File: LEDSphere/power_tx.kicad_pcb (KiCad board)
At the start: 2 copper layers, 124 x 120 mm, 90 parts, among them J1 USB_C_Receptacle_USB2.0, M1 Motor_DC, Q1 BSS138, Q2 BSS138, Q3 BSS138, Q4 BSS138, Q5 BSS138, Q6 BSS138, Q7 Si2319CDS, Q8 Si2319CDS, U1 4017, U2 CH221K, U3 TPS54302, U4 SG3525, U8 UCC27714DR

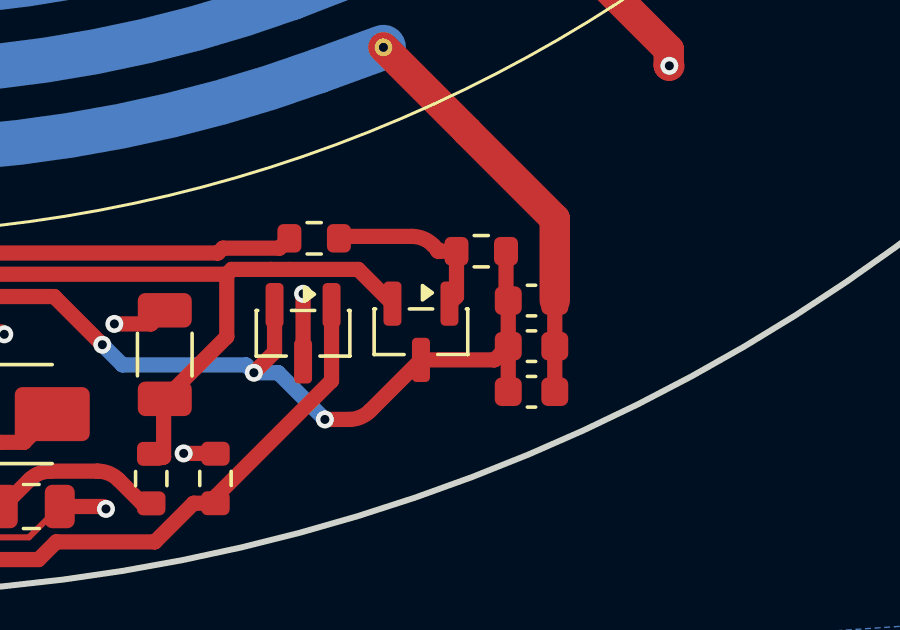
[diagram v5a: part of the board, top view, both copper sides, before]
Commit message: Updated Resonance FRQ + Test Points Added
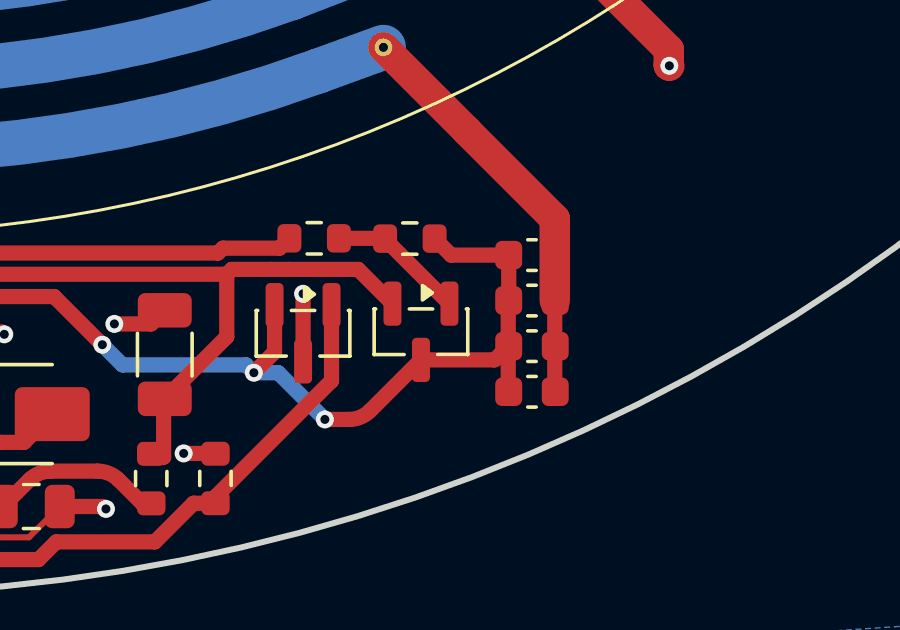
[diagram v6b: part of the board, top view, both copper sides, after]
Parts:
- added C29: 68nF, Capacitor_SMD:C_0603_1608Metric, F.Cu at (159.6, 144.8)
- L2: value 8.1 uH -> 5.8 uH
- moved R31 2.42 mm to (155.5, 144.3)
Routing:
- net /HS: track 47.7 -> 50.2 mm
- net /FET_HI: track 6.00 -> 4.60 mm

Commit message: Most Recent TX Board Changes
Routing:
- net +12V: track 184.6 -> 158.8 mm
- net Net-(U8-LI): track 1.88 -> 7.59 mm

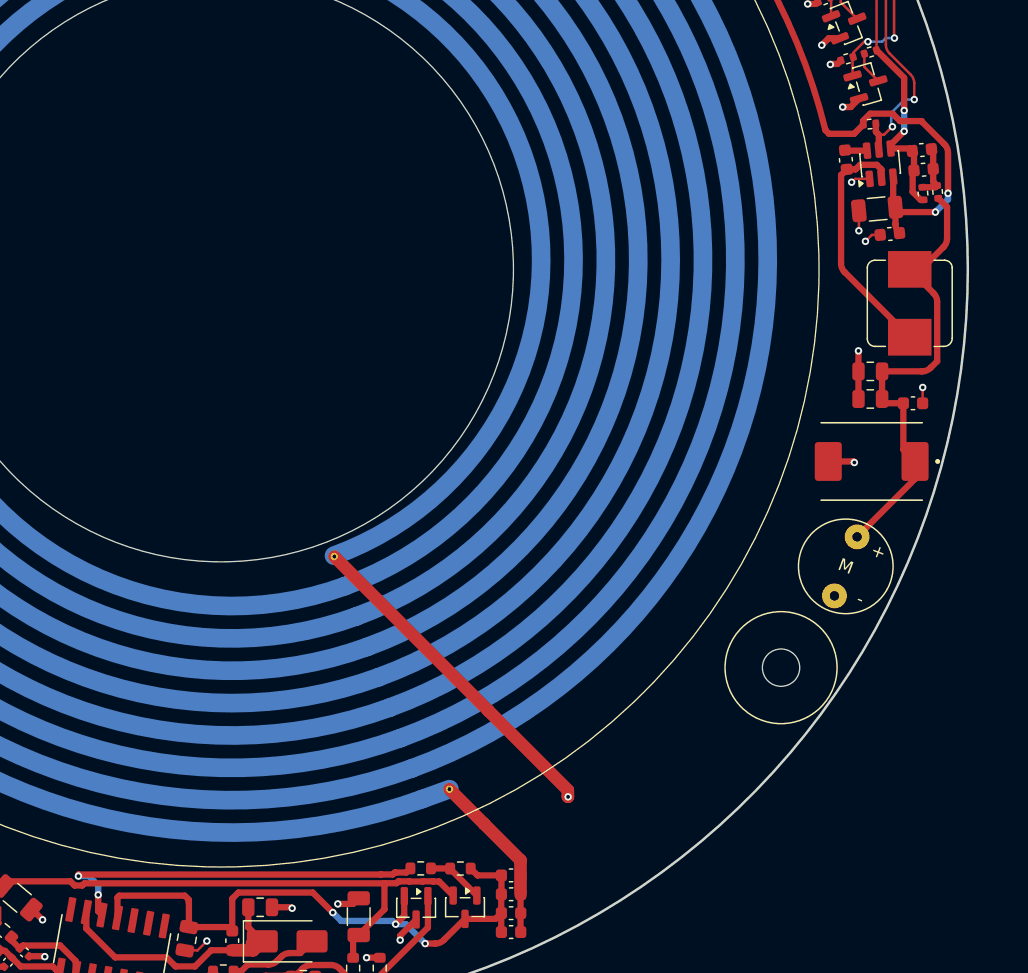
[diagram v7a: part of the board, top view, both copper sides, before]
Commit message: Minor Layout Changes for TX Board
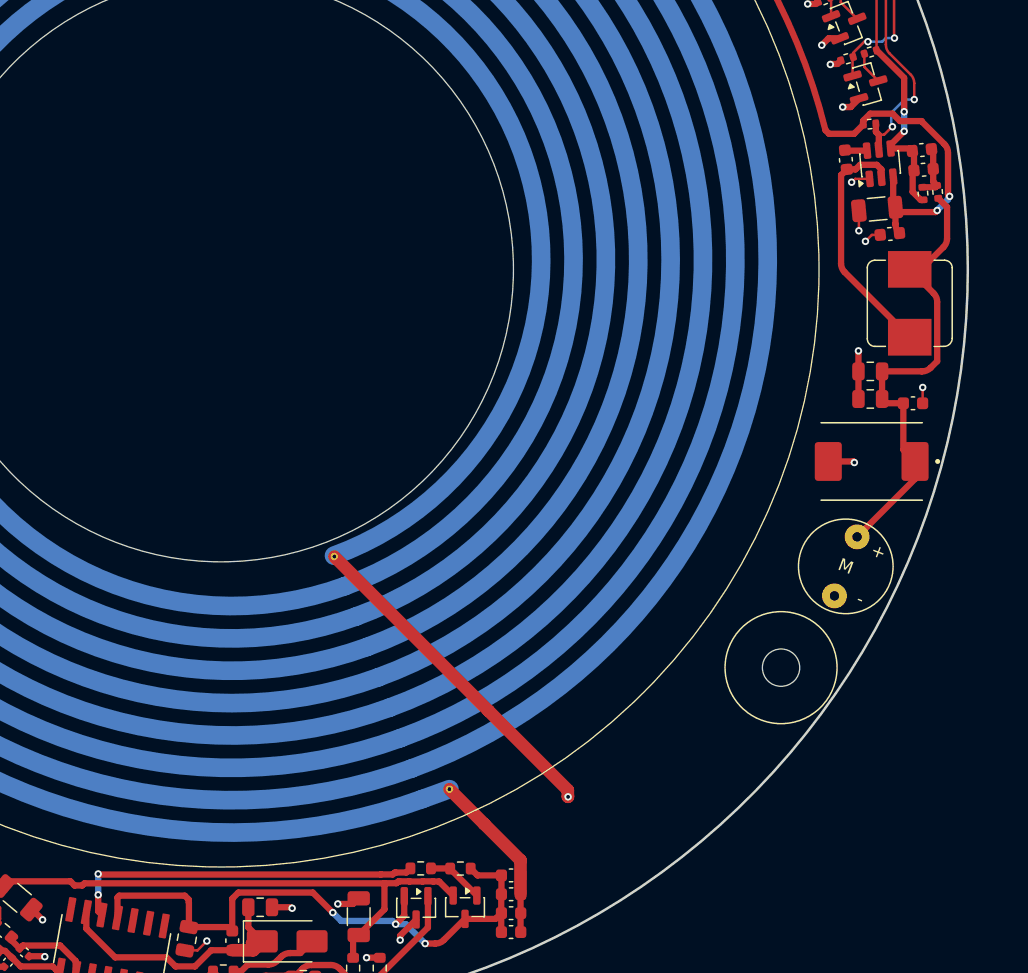
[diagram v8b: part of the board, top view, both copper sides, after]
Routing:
- net Net-(U8-HO): track 31.4 -> 28.7 mm
